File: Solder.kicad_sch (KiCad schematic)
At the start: 5 parts

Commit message: Finished? :D
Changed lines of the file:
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@@
-	)
-	(symbol
-		(lib_id "power:GND")
-		(at 142.24 57.15 0)
-		(unit 1)
-		(exclude_from_sim no)
-		(in_bom yes)
-		(on_board yes)
-		(dnp no)
-		(fields_autoplaced yes)
-		(property "Reference" "#PWR01"
-			(at 142.24 63.5 0)
-			(effects
-				(font
-					(size 1.27 1.27)
-				)
-				(hide yes)
-			)
-		)
-		(property "Value" "GND"
-			(at 142.24 62.23 0)
-			(effects
-				(font
-					(size 1.27 1.27)
-				)
-			)
-		)
-		(property "Footprint" ""
-			(at 142.24 57.15 0)
-			(effects
-				(font
-					(size 1.27 1.27)
-				)
-				(hide yes)
-			)
-		)
-		(property "Datasheet" ""
-			(at 142.24 57.15 0)
-			(effects
-				(font
-					(size 1.27 1.27)
-				)
-				(hide yes)
-			)
-		)
-		(property "Description" "Power symbol creates a global label with name \"GND\" , ground"
-			(at 142.24 57.15 0)
-			(effects
-				(font
-					(size 1.27 1.27)
-				)
-				(hide yes)
-			)
-		)
-		(pin "1"
-		)
-		(instances
-			(project ""
-				(path "/8b732828-8244-451f-9bdb-50d32063189d"
-					(reference "#PWR01")
-					(unit 1)
-				)
-			)
-		)
 	)
 	(symbol

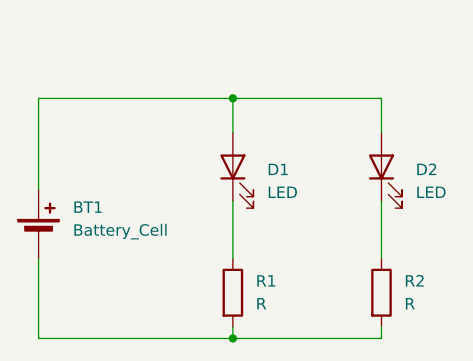
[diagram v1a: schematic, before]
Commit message: Add a button
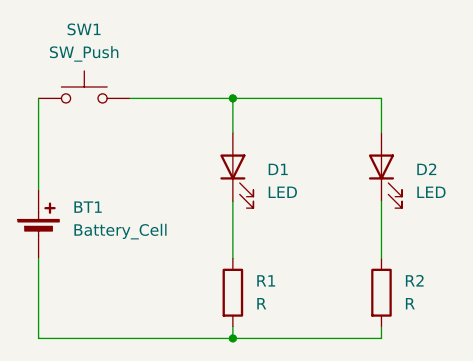
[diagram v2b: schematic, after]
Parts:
- added SW1: SW_Push, Button_Switch_THT:SW_PUSH_6mm, symbol Switch:SW_Push
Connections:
- net at D1.2 (A), D2.2 (A): now also SW1.2; no longer BT1.1 (+)
- new net: BT1.1 (+), SW1.1
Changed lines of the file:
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@@
-	(wire
-		(pts
-			(xy 105.41 63.5) (xy 127 63.5)
-		)
-		(stroke
-			(width 0)
-			(type default)
-		)
-	)
 	(wire
 		(pts
@@
 		(pts
 			(xy 143.51 63.5) (xy 143.51 67.31)
+		)
+		(stroke
+			(width 0)
+			(type default)
+		)
+	)
+	(wire
+		(pts
+			(xy 115.57 63.5) (xy 127 63.5)
 		)
 		(stroke
@@
 					(unit 1)
 				)
+			)
+		)
+	)
+	(symbol
+		(lib_id "Switch:SW_Push")
+		(at 110.49 63.5 0)
+		(unit 1)
+		(exclude_from_sim no)
+		(in_bom yes)
+		(on_board yes)
+		(dnp no)
+		(fields_autoplaced yes)
+		(property "Reference" "SW1"
+			(at 110.49 55.88 0)
+			(effects
+				(font
+					(size 1.27 1.27)
+				)
+			)
+		)
+		(property "Value" "SW_Push"
+			(at 110.49 58.42 0)
+			(effects
+				(font
+					(size 1.27 1.27)
+				)
+			)
+		)
+		(property "Footprint" "Button_Switch_THT:SW_PUSH_6mm"
+			(at 110.49 58.42 0)
+			(effects
+				(font
+					(size 1.27 1.27)
+				)
+				(hide yes)
+			)
+		)
+		(property "Datasheet" "~"
+			(at 110.49 58.42 0)
+			(effects
+				(font
+					(size 1.27 1.27)
+				)
+				(hide yes)
+			)
+		)
+		(property "Description" "Push button switch, generic, two pins"
+			(at 110.49 63.5 0)
+			(effects
+				(font
+					(size 1.27 1.27)
+				)
+				(hide yes)
+			)
+		)
+		(pin "2"
+		)
+		(pin "1"
+		)
+		(instances
+			(project ""
+				(path "/8b732828-8244-451f-9bdb-50d32063189d"
+					(reference "SW1")
+					(unit 1)
+				)
